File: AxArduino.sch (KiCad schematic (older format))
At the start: 31 parts, among them P1 CONN_01X02, P10 CONN_01X04, P11 CONN_01X04, P2 CONN_01X02, P3 CONN_01X03, P4 CONN_01X03, P5 CONN_01X03, P7 CONN_01X03, P8 CONN_01X15, P9 CONN_01X15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

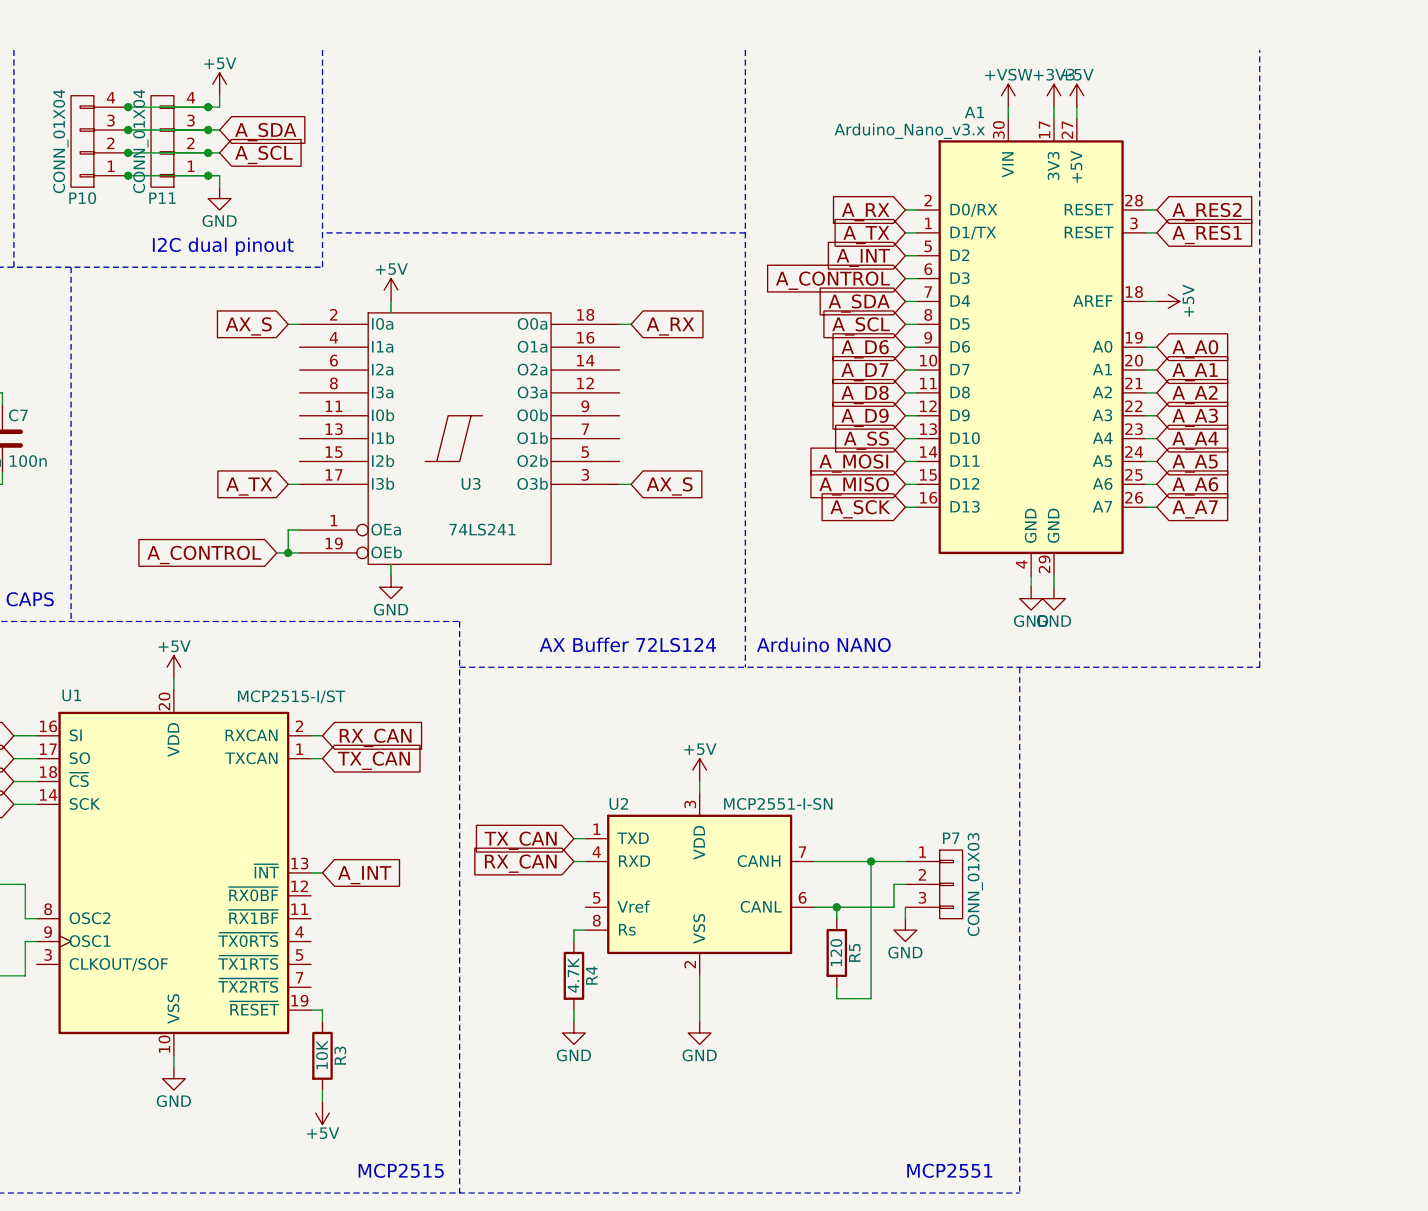
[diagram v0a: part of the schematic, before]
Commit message: Fixed stuff, like moving r to top layer and adding pullups to i2c
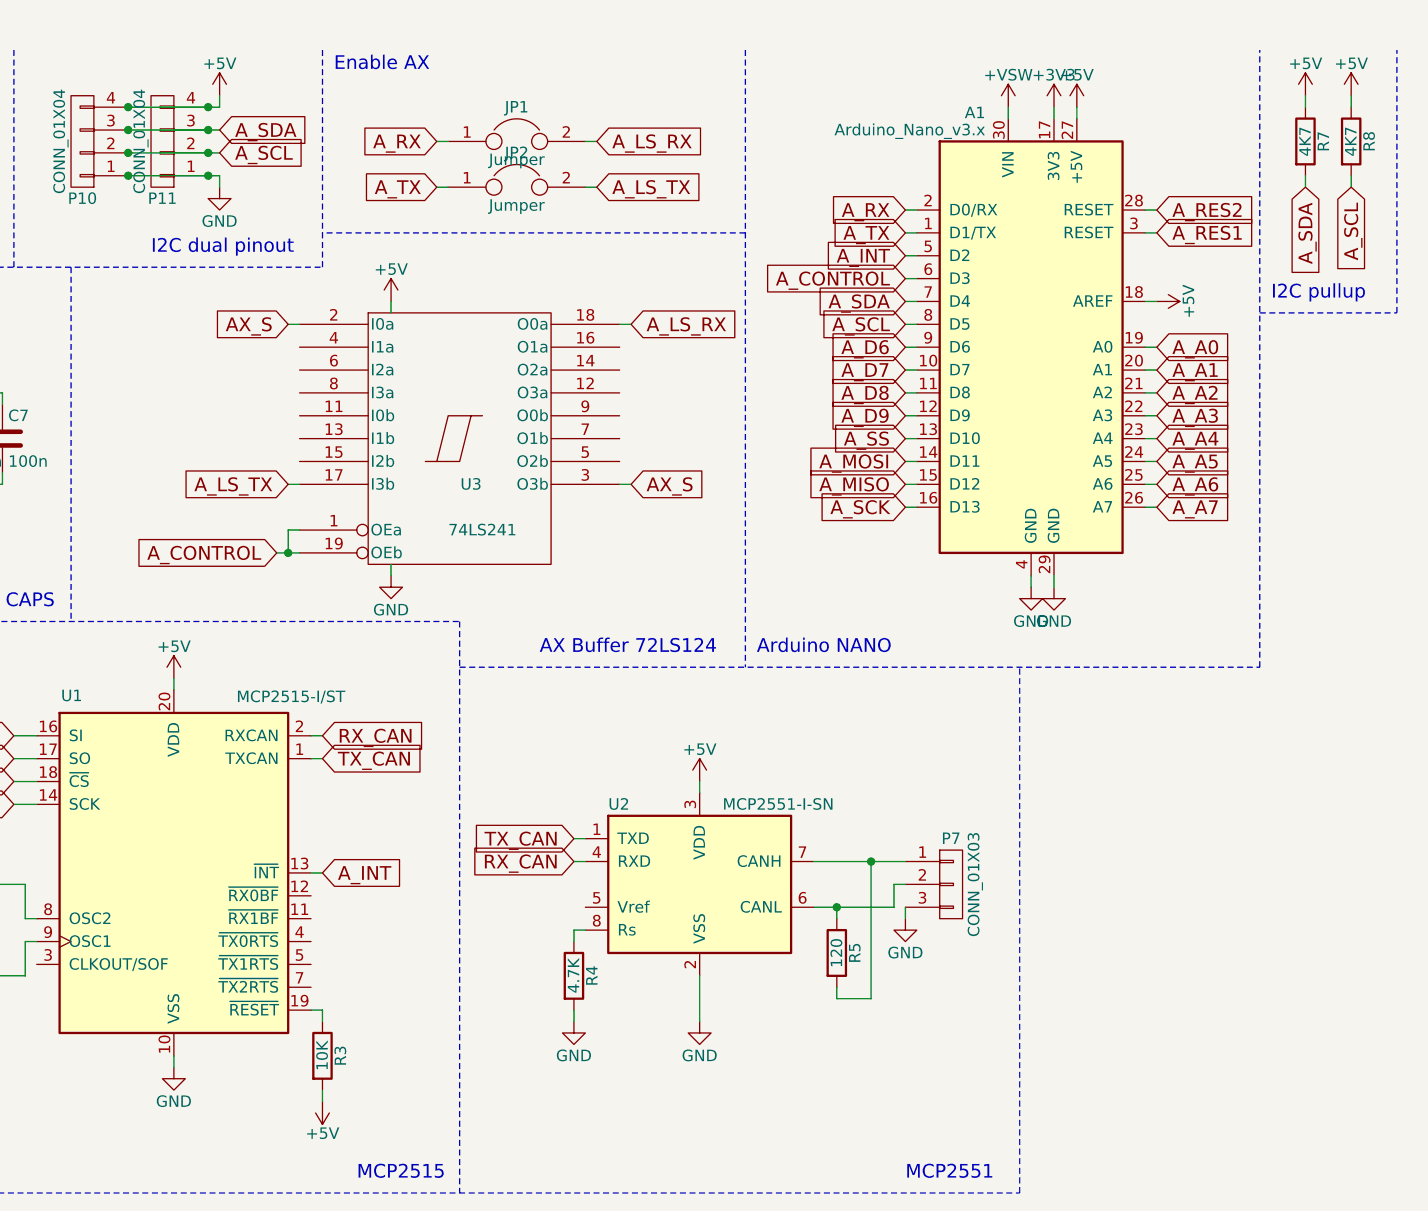
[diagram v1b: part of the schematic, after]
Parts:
- added JP1, JP2: Jumper, Pin_Headers:Pin_Header_Straight_1x02_Pitch2.54mm, symbol Jumper
- added R7, R8: 4K7, Resistors_SMD:R_0805, symbol R
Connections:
- net +5V: now also R7.1, R8.1
- net A_RX: now also JP1.1; no longer U3.18 (O0a)
- net A_SCL: now also R8.2
- net A_SDA: now also R7.2
- net A_TX: now also JP2.1; no longer U3.17 (I3b)
- new net A_LS_RX: JP1.2, U3.18 (O0a)
- new net A_LS_TX: JP2.2, U3.17 (I3b)
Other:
- note added: "Enable AX"
- note added: "I2C pullup\n"

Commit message: New design
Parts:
- removed C3, C4: C, Capacitors_SMD:C_0805, symbol C
- removed P10: CONN_01X04, Pin_Headers:Pin_Header_Straight_1x04, symbol CONN_01X04
- removed R3: 10K, Resistors_SMD:R_0805, symbol R
- removed R4: 4.7K, Resistors_SMD:R_0805, symbol R
- removed R5: 120, Resistors_SMD:R_0805, symbol R
- removed U1: MCP2515-I/ST, Housings_SSOP:TSSOP-20_4.4x6.5mm_Pitch0.65mm, symbol MCP2515-I/ST
- removed U2: MCP2551-I-SN, Housings_SOIC:SOIC-8_3.9x4.9mm_Pitch1.27mm, symbol MCP2551-I-SN
- removed Y1: Crystal, Crystals:Crystal_HC49-U_Vertical, symbol Crystal
- added C3: CP, Capacitors_SMD:CP_Elec_6.3x5.3, symbol CP
- added P12: CONN_01X03, Pin_Headers:Pin_Header_Straight_1x03_Pitch2.54mm, symbol CONN_01X03
- added P6: CONN_01X02, Connectors_Terminal_Blocks:TerminalBlock_Pheonix_MKDS1.5-2pol, symbol CONN_01X02
- C1, C2: footprint Capacitors_SMD:c_elec_6.3x5.3 -> Capacitors_SMD:CP_Elec_6.3x5.3
- P1, P2: footprint Terminal_Blocks:TerminalBlock_Pheonix_MPT-2.54mm_2pol -> Connectors_Terminal_Blocks:TerminalBlock_Pheonix_MKDS1.5-2pol
- P11: footprint Pin_Headers:Pin_Header_Straight_1x04 -> Pin_Headers:Pin_Header_Straight_1x04_Pitch2.54mm
- P3, P4, P5, P7: footprint Pin_Headers:Pin_Header_Straight_1x03 -> Pin_Headers:Pin_Header_Straight_1x03_Pitch2.54mm
- P8, P9: footprint Pin_Headers:Pin_Header_Straight_1x15 -> Pin_Headers:Pin_Header_Straight_1x15_Pitch2.54mm
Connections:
- net A_D8 is gone; now on net A_CONTROL: A1.11 (D8), P8.11 (P11)
- net AX_P: no longer P5.1 (P1)
- net AX_S: no longer P5.2 (P2)
- net A_A1: now also P7.1 (P1), C3.1, P12.1 (P1), P6.2 (P2)
- net A_CONTROL: no longer A1.6 (D3), P8.6 (P6)
- net A_D6: now also P7.2 (P2)
- net A_D9: now also P12.2 (P2)
- net A_MOSI: now also P5.2 (P2)
- net A_SS: now also P5.3 (P3)
- net GND: now also P5.1 (P1), C3.2, P12.3 (P3), P6.1 (P1); no longer P5.3 (P3)
- new net A_D3: A1.6 (D3), P8.6 (P6)
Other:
- note added: "!WARNING!\n- while programming disconnect jumper for AX EN\n- servo has no protection, watch out!\n"
- note added: "2x Servo PWM pinouts"
- note added: "Arduino Nano extension boad \nwith AX-12 servo power and communication included"
- note added: "SS RX"
- note added: "SS TX"
- note added: "UART Communication \nSoft Serial"
- note removed: "MCP2515"
- note removed: "MCP2551"
- moved on the sheet: P11

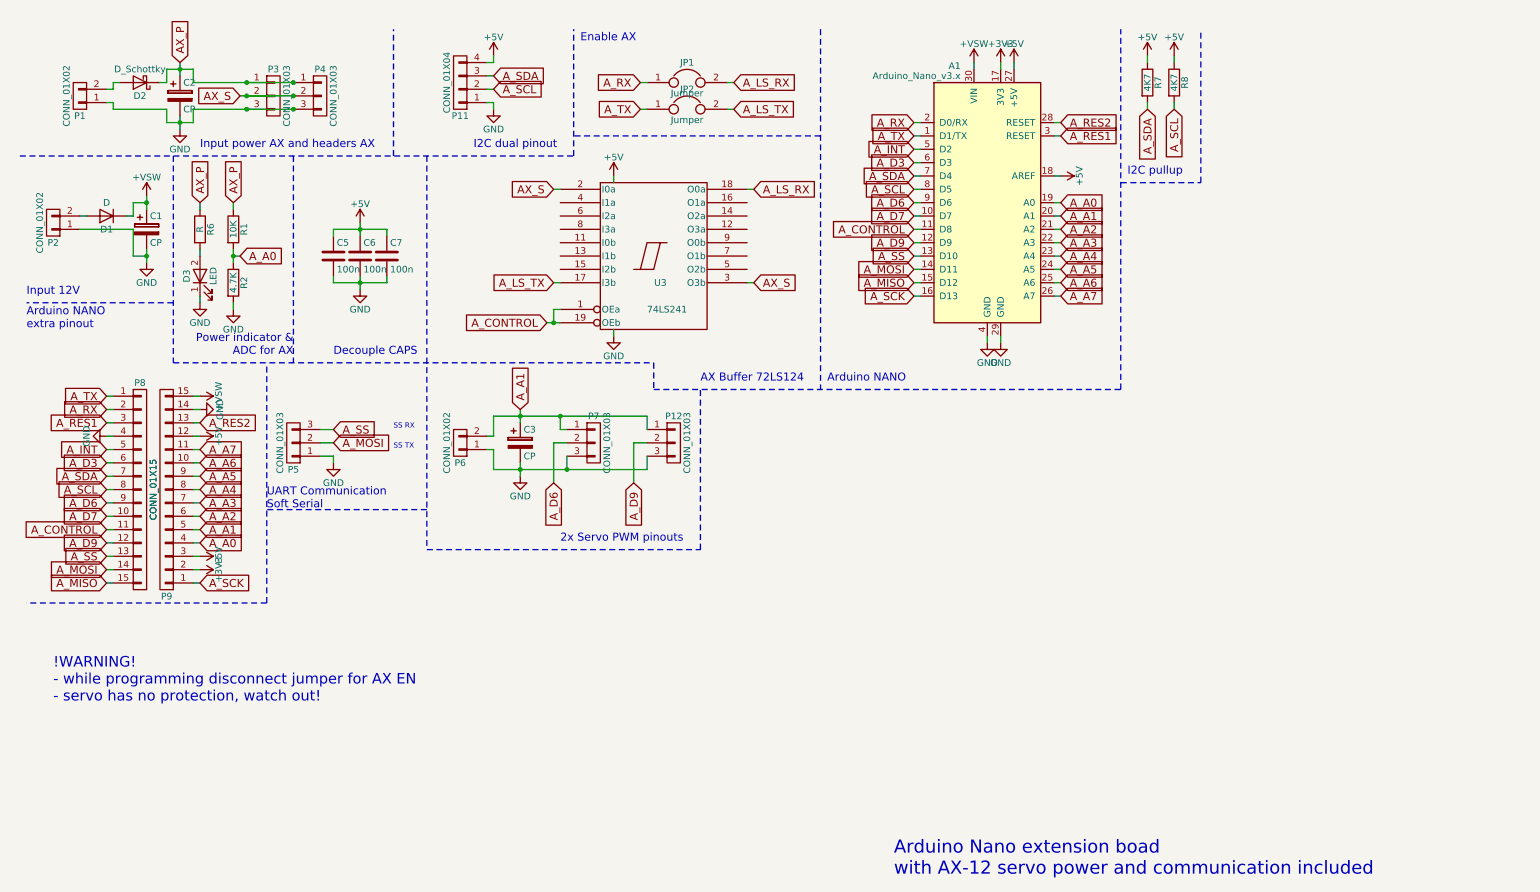
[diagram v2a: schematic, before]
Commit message: Small modifs, added connectors and servo support
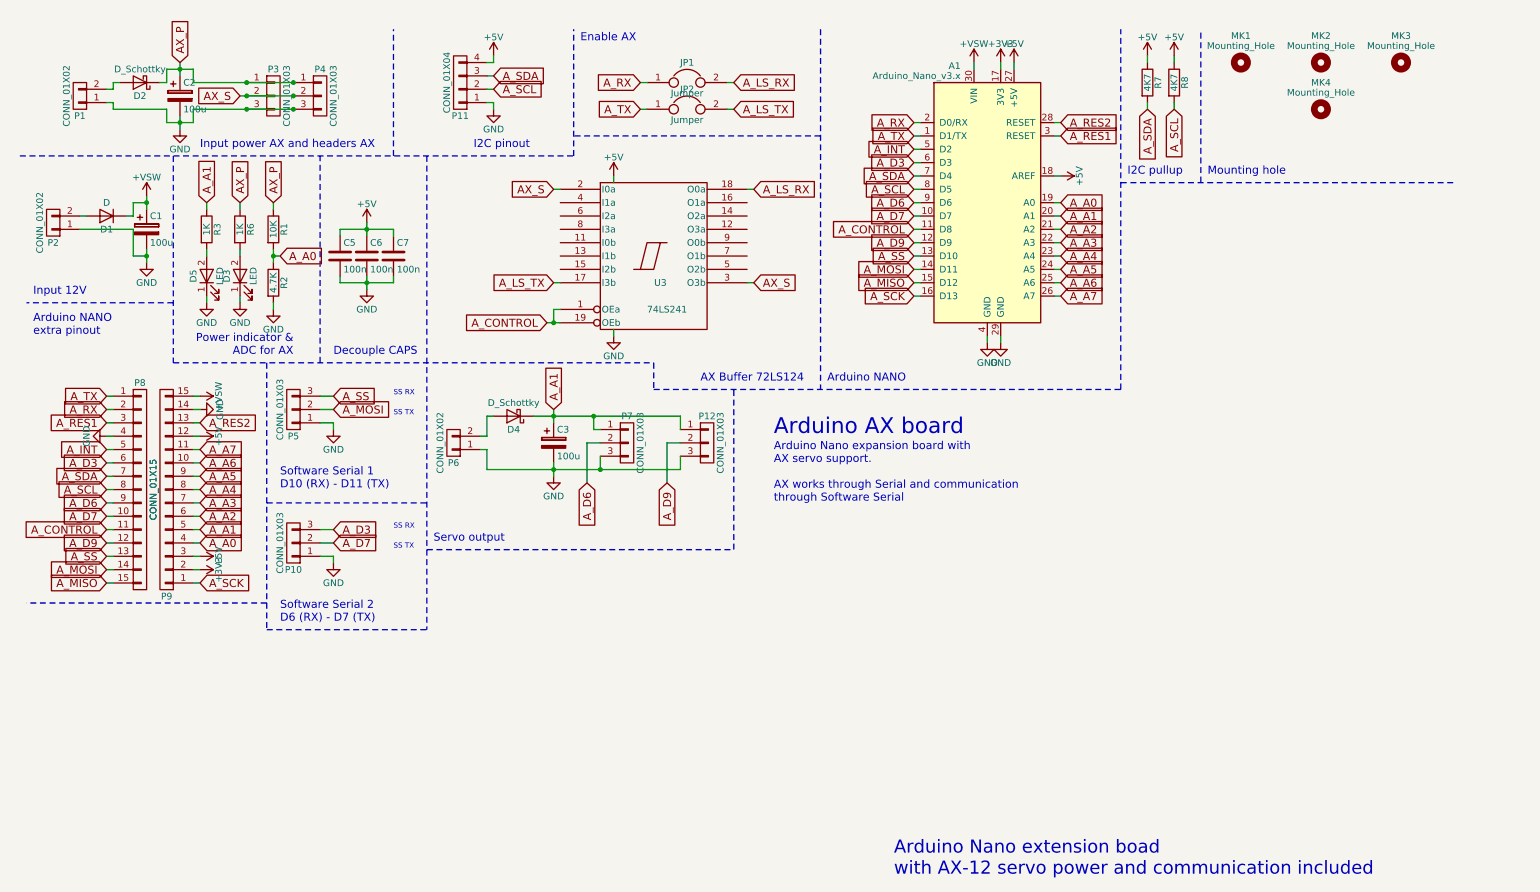
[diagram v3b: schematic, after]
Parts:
- added D4: D_Schottky, Diodes_SMD:D_SMB_Standard, symbol D_Schottky
- added D5: LED, LEDs:LED_0805, symbol LED
- added MK1, MK2: Mounting_Hole, Mounting_Holes:MountingHole_3.2mm_M3_Pad_Via, symbol Mounting_Hole
- added MK3, MK4: Mounting_Hole, Mounting_Holes:MountingHole_2.2mm_M2_Pad, symbol Mounting_Hole
- added P10: CONN_01X03, Pin_Headers:Pin_Header_Straight_1x03_Pitch2.54mm, symbol CONN_01X03
- added R3: 1K, Resistors_SMD:R_0805, symbol R
- C1, C2, C3: value CP -> 100u
- R6: value R -> 1K
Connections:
- net A_A1: now also D4.1 (K), R3.1; no longer P6.2 (P2)
- net A_D3: now also P10.3 (P3)
- net A_D7: now also P10.2 (P2)
- net GND: now also D5.1 (K), P10.1 (P1)
- new net: D4.2 (A), P6.2 (P2)
- new net: D5.2 (A), R3.2
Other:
- note added: "Arduino AX board"
- note added: "Arduino Nano expansion board with \nAX servo support.\n\nAX works through Serial and communication\nthrough Software Serial"
- note added: "I2C pinout"
- note added: "Mounting hole\n"
- note added: "Servo output"
- note added: "Software Serial 1\nD10 (RX) - D11 (TX)"
- note added: "Software Serial 2\nD6 (RX) - D7 (TX)"
- note removed: "!WARNING!\n- while programming disconnect jumper for AX EN\n- servo has no protection, watch out!\n"
- note removed: "2x Servo PWM pinouts"
- note removed: "I2C dual pinout"
- note removed: "UART Communication \nSoft Serial"
- moved on the sheet: C3, C5, C6, C7, D3, P12, P5, P6, P7, R1, R2, R6
